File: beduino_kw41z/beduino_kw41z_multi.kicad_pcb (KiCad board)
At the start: 2 copper layers, 81 x 100 mm, 336 parts, among them J1 USB_OTG, J2 Conn_01x07, J3 Conn_01x07, Q1 Q_PMOS_SGD, SW1 SW_Push, SW2 Reset, U1 TC1017, U2 LPC11U35FHI33-501, U3 TC1017, U4 Module_CONN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

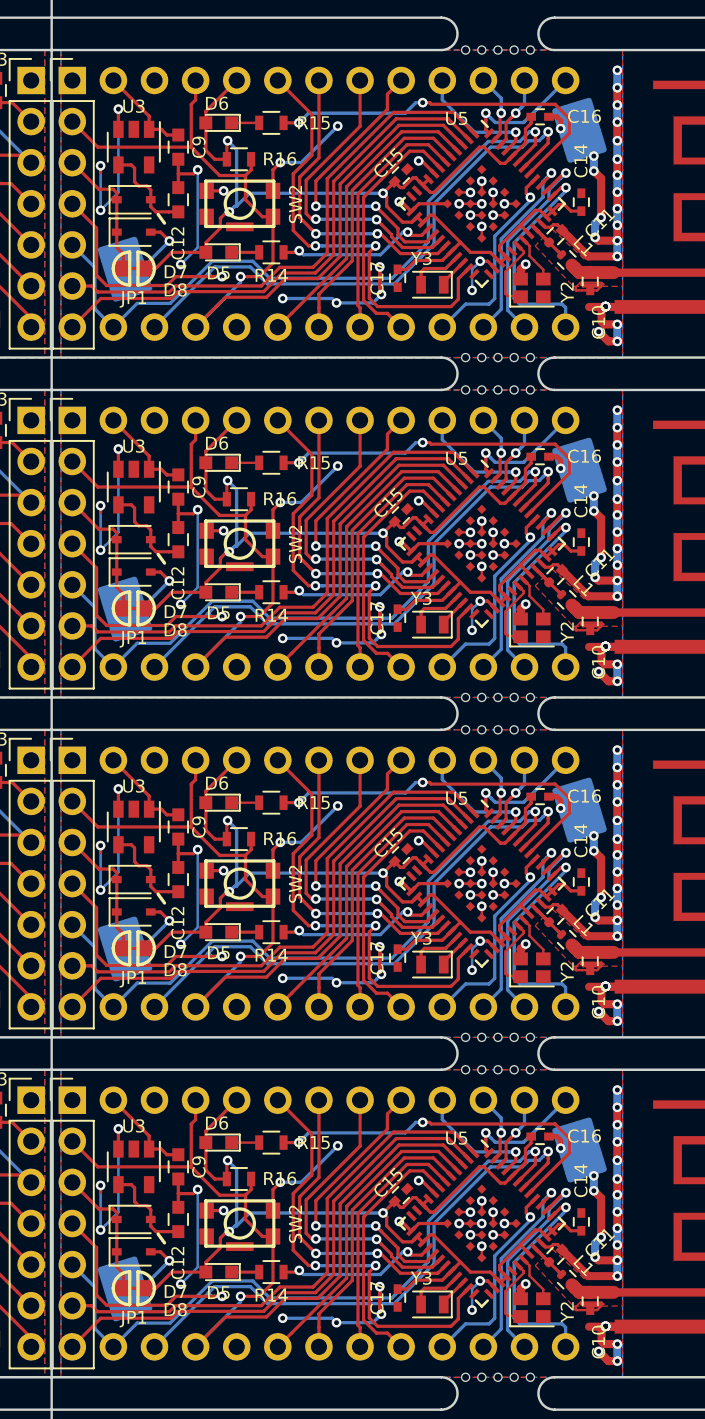
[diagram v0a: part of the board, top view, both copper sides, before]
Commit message: Update board design to be kicad v4 compatible again.
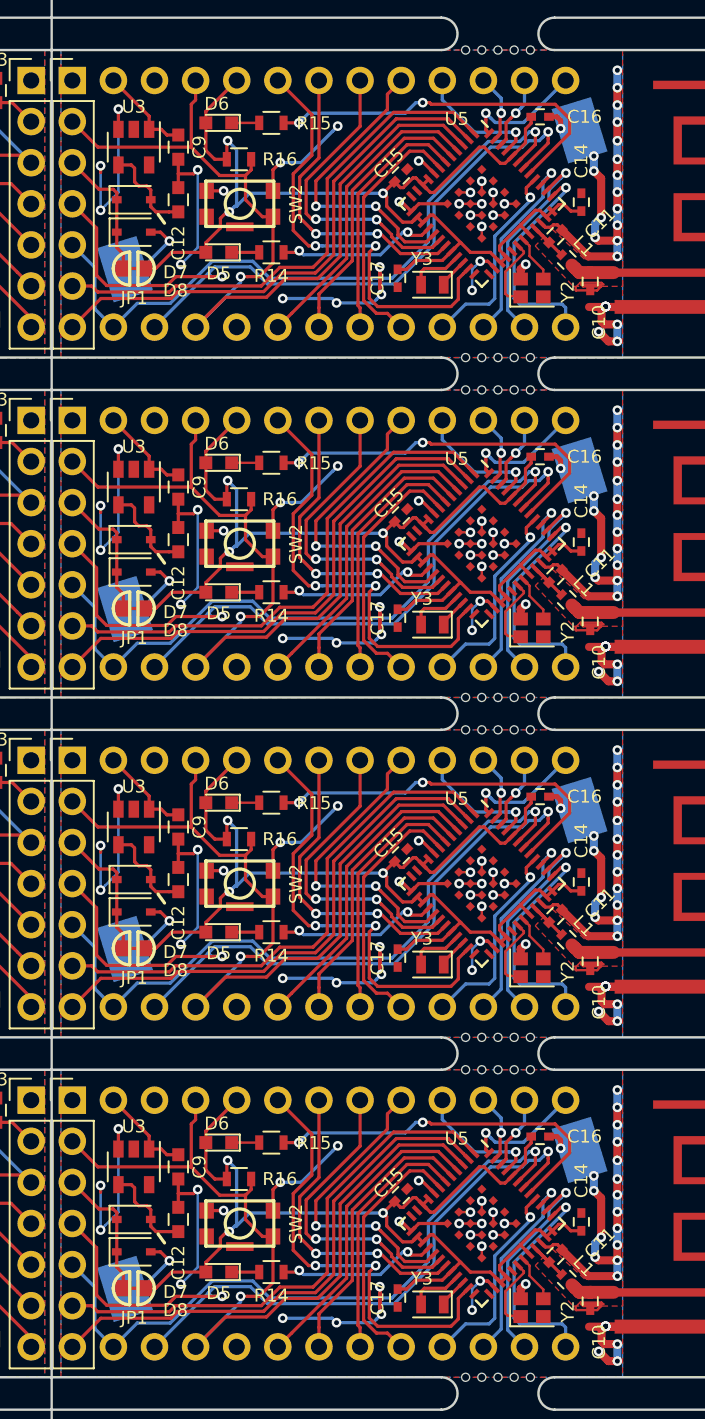
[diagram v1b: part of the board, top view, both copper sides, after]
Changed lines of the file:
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@@
     (fp_arc (start 0 0) (end -11.06 4.11) (angle -139.2) (layer B.CrtYd) (width 0.05))
     (fp_arc (start 0 0) (end 11.06 -4.11) (angle -139.2) (layer B.CrtYd) (width 0.05))
-    (pad 2 smd roundrect (at 14.68 0 17) (size 2.54 3.51) (layers B.Cu B.Paste B.Mask)(roundrect_rratio 0.07000000000000001)
+    (pad 2 smd rect (at 14.68 0 17) (size 2.54 3.51) (layers B.Cu B.Paste B.Mask)
       (zone_connect 2) (thermal_width 3.5) (thermal_gap 0.4))
-    (pad 1 smd roundrect (at -14.68 0 17) (size 2.54 3.51) (layers B.Cu B.Paste B.Mask)(roundrect_rratio 0.07000000000000001))
+    (pad 1 smd rect (at -14.68 0 17) (size 2.54 3.51) (layers B.Cu B.Paste B.Mask))
   )
   (module Housings_DFN_QFN:QFN-48-1EP_7x7mm_Pitch0.5mm (layer F.Cu)
@@
     (pad 1 smd rect (at -1.3 -1.35) (size 1.35 0.4) (layers F.Cu F.Paste F.Mask))
     (model ${KISYS3DMOD}/Connectors_USB.3dshapes/USB_Micro-B_Molex_47346-0001.step
-      (offset (xyz 0 -1.4 0))
+      (at (xyz 0 -1.4 0))
       (scale (xyz 1 1 1))
       (rotate (xyz 0 0 0))
@@
     (fp_line (start 1 0.4) (end 1 -0.4) (layer F.CrtYd) (width 0.05))
     (fp_line (start 1 0.4) (end -1 0.4) (layer F.CrtYd) (width 0.05))
-    (pad 1 smd roundrect (at -0.55 0 45) (size 0.6 0.5) (layers F.Cu F.Paste F.Mask)(roundrect_rratio 0.35))
+    (pad 1 smd rect (at -0.55 0 45) (size 0.6 0.5) (layers F.Cu F.Paste F.Mask))
     (pad 2 smd rect (at 0.55 0 45) (size 0.6 0.5) (layers F.Cu F.Paste F.Mask))
     (model Capacitors_SMD.3dshapes/C_0402.wrl
@@
     (fp_line (start 1 0.4) (end 1 -0.4) (layer F.CrtYd) (width 0.05))
     (fp_line (start 1 0.4) (end -1 0.4) (layer F.CrtYd) (width 0.05))
-    (pad 1 smd roundrect (at -0.55 0 270) (size 0.6 0.5) (layers F.Cu F.Paste F.Mask)(roundrect_rratio 0.35))
+    (pad 1 smd rect (at -0.55 0 270) (size 0.6 0.5) (layers F.Cu F.Paste F.Mask))
     (pad 2 smd rect (at 0.55 0 270) (size 0.6 0.5) (layers F.Cu F.Paste F.Mask))
     (model Capacitors_SMD.3dshapes/C_0402.wrl
@@
     (fp_line (start 0.25 -0.53) (end -0.25 -0.53) (layer F.SilkS) (width 0.12))
     (fp_line (start -0.25 0.53) (end 0.25 0.53) (layer F.SilkS) (width 0.12))
-    (pad 1 smd roundrect (at -0.45 0 315) (size 0.4 0.6) (layers F.Cu F.Paste F.Mask)(roundrect_rratio 0.35))
-    (pad 2 smd roundrect (at 0.45 0 315) (size 0.4 0.6) (layers F.Cu F.Paste F.Mask)(roundrect_rratio 0.35))
+    (pad 1 smd rect (at -0.45 0 315) (size 0.4 0.6) (layers F.Cu F.Paste F.Mask))
+    (pad 2 smd rect (at 0.45 0 315) (size 0.4 0.6) (layers F.Cu F.Paste F.Mask))
     (model ${KISYS3DMOD}/Inductors_SMD.3dshapes/L_0402.wrl
       (at (xyz 0 0 0))
@@
     (fp_arc (start 0 0) (end -11.06 4.11) (angle -139.2) (layer B.CrtYd) (width 0.05))
     (fp_arc (start 0 0) (end 11.06 -4.11) (angle -139.2) (layer B.CrtYd) (width 0.05))
-    (pad 2 smd roundrect (at 14.68 0 17) (size 2.54 3.51) (layers B.Cu B.Paste B.Mask)(roundrect_rratio 0.07000000000000001)
+    (pad 2 smd rect (at 14.68 0 17) (size 2.54 3.51) (layers B.Cu B.Paste B.Mask)
       (zone_connect 2) (thermal_width 3.5) (thermal_gap 0.4))
-    (pad 1 smd roundrect (at -14.68 0 17) (size 2.54 3.51) (layers B.Cu B.Paste B.Mask)(roundrect_rratio 0.07000000000000001))
+    (pad 1 smd rect (at -14.68 0 17) (size 2.54 3.51) (layers B.Cu B.Paste B.Mask))
   )
   (module Housings_DFN_QFN:QFN-48-1EP_7x7mm_Pitch0.5mm (layer F.Cu)
@@
     (pad 1 smd rect (at -1.3 -1.35) (size 1.35 0.4) (layers F.Cu F.Paste F.Mask))
     (model ${KISYS3DMOD}/Connectors_USB.3dshapes/USB_Micro-B_Molex_47346-0001.step
-      (offset (xyz 0 -1.4 0))
+      (at (xyz 0 -1.4 0))
       (scale (xyz 1 1 1))
       (rotate (xyz 0 0 0))
@@
     (fp_line (start 1 0.4) (end 1 -0.4) (layer F.CrtYd) (width 0.05))
     (fp_line (start 1 0.4) (end -1 0.4) (layer F.CrtYd) (width 0.05))
-    (pad 1 smd roundrect (at -0.55 0 45) (size 0.6 0.5) (layers F.Cu F.Paste F.Mask)(roundrect_rratio 0.35))
+    (pad 1 smd rect (at -0.55 0 45) (size 0.6 0.5) (layers F.Cu F.Paste F.Mask))
     (pad 2 smd rect (at 0.55 0 45) (size 0.6 0.5) (layers F.Cu F.Paste F.Mask))
     (model Capacitors_SMD.3dshapes/C_0402.wrl
@@
     (fp_line (start 1 0.4) (end 1 -0.4) (layer F.CrtYd) (width 0.05))
     (fp_line (start 1 0.4) (end -1 0.4) (layer F.CrtYd) (width 0.05))
-    (pad 1 smd roundrect (at -0.55 0 270) (size 0.6 0.5) (layers F.Cu F.Paste F.Mask)(roundrect_rratio 0.35))
+    (pad 1 smd rect (at -0.55 0 270) (size 0.6 0.5) (layers F.Cu F.Paste F.Mask))
     (pad 2 smd rect (at 0.55 0 270) (size 0.6 0.5) (layers F.Cu F.Paste F.Mask))
     (model Capacitors_SMD.3dshapes/C_0402.wrl
@@
     (fp_line (start 0.25 -0.53) (end -0.25 -0.53) (layer F.SilkS) (width 0.12))
     (fp_line (start -0.25 0.53) (end 0.25 0.53) (layer F.SilkS) (width 0.12))
-    (pad 1 smd roundrect (at -0.45 0 315) (size 0.4 0.6) (layers F.Cu F.Paste F.Mask)(roundrect_rratio 0.35))
-    (pad 2 smd roundrect (at 0.45 0 315) (size 0.4 0.6) (layers F.Cu F.Paste F.Mask)(roundrect_rratio 0.35))
+    (pad 1 smd rect (at -0.45 0 315) (size 0.4 0.6) (layers F.Cu F.Paste F.Mask))
+    (pad 2 smd rect (at 0.45 0 315) (size 0.4 0.6) (layers F.Cu F.Paste F.Mask))
     (model ${KISYS3DMOD}/Inductors_SMD.3dshapes/L_0402.wrl
       (at (xyz 0 0 0))
@@
     (fp_arc (start 0 0) (end -11.06 4.11) (angle -139.2) (layer B.CrtYd) (width 0.05))
     (fp_arc (start 0 0) (end 11.06 -4.11) (angle -139.2) (layer B.CrtYd) (width 0.05))
-    (pad 2 smd roundrect (at 14.68 0 17) (size 2.54 3.51) (layers B.Cu B.Paste B.Mask)(roundrect_rratio 0.07000000000000001)
+    (pad 2 smd rect (at 14.68 0 17) (size 2.54 3.51) (layers B.Cu B.Paste B.Mask)
       (zone_connect 2) (thermal_width 3.5) (thermal_gap 0.4))
-    (pad 1 smd roundrect (at -14.68 0 17) (size 2.54 3.51) (layers B.Cu B.Paste B.Mask)(roundrect_rratio 0.07000000000000001))
+    (pad 1 smd rect (at -14.68 0 17) (size 2.54 3.51) (layers B.Cu B.Paste B.Mask))
   )
   (module Housings_DFN_QFN:QFN-48-1EP_7x7mm_Pitch0.5mm (layer F.Cu)
@@
     (pad 1 smd rect (at -1.3 -1.35) (size 1.35 0.4) (layers F.Cu F.Paste F.Mask))
     (model ${KISYS3DMOD}/Connectors_USB.3dshapes/USB_Micro-B_Molex_47346-0001.step
-      (offset (xyz 0 -1.4 0))
+      (at (xyz 0 -1.4 0))
       (scale (xyz 1 1 1))
       (rotate (xyz 0 0 0))
@@
     (fp_line (start 1 0.4) (end 1 -0.4) (layer F.CrtYd) (width 0.05))
     (fp_line (start 1 0.4) (end -1 0.4) (layer F.CrtYd) (width 0.05))
-    (pad 1 smd roundrect (at -0.55 0 45) (size 0.6 0.5) (layers F.Cu F.Paste F.Mask)(roundrect_rratio 0.35))
+    (pad 1 smd rect (at -0.55 0 45) (size 0.6 0.5) (layers F.Cu F.Paste F.Mask))
     (pad 2 smd rect (at 0.55 0 45) (size 0.6 0.5) (layers F.Cu F.Paste F.Mask))
     (model Capacitors_SMD.3dshapes/C_0402.wrl
@@
     (fp_line (start 1 0.4) (end 1 -0.4) (layer F.CrtYd) (width 0.05))
     (fp_line (start 1 0.4) (end -1 0.4) (layer F.CrtYd) (width 0.05))
-    (pad 1 smd roundrect (at -0.55 0 270) (size 0.6 0.5) (layers F.Cu F.Paste F.Mask)(roundrect_rratio 0.35))
+    (pad 1 smd rect (at -0.55 0 270) (size 0.6 0.5) (layers F.Cu F.Paste F.Mask))
     (pad 2 smd rect (at 0.55 0 270) (size 0.6 0.5) (layers F.Cu F.Paste F.Mask))
     (model Capacitors_SMD.3dshapes/C_0402.wrl
@@
     (fp_line (start 0.25 -0.53) (end -0.25 -0.53) (layer F.SilkS) (width 0.12))
     (fp_line (start -0.25 0.53) (end 0.25 0.53) (layer F.SilkS) (width 0.12))
-    (pad 1 smd roundrect (at -0.45 0 315) (size 0.4 0.6) (layers F.Cu F.Paste F.Mask)(roundrect_rratio 0.35))
-    (pad 2 smd roundrect (at 0.45 0 315) (size 0.4 0.6) (layers F.Cu F.Paste F.Mask)(roundrect_rratio 0.35))
+    (pad 1 smd rect (at -0.45 0 315) (size 0.4 0.6) (layers F.Cu F.Paste F.Mask))
+    (pad 2 smd rect (at 0.45 0 315) (size 0.4 0.6) (layers F.Cu F.Paste F.Mask))
     (model ${KISYS3DMOD}/Inductors_SMD.3dshapes/L_0402.wrl
       (at (xyz 0 0 0))
@@
     (fp_arc (start 0 0) (end -10.61275 3.5) (angle -27.4635) (layer B.Fab) (width 0.1))
     (fp_circle (center 0 0) (end 10 0) (layer Dwgs.User) (width 0.15))
-    (pad 1 smd roundrect (at -14.68 0 17) (size 2.54 3.51) (layers B.Cu B.Paste B.Mask)(roundrect_rratio 0.07000000000000001)
+    (pad 1 smd rect (at -14.68 0 17) (size 2.54 3.51) (layers B.Cu B.Paste B.Mask)
       (net 3 "Net-(BT1-Pad1)"))
-    (pad 2 smd roundrect (at 14.68 0 17) (size 2.54 3.51) (layers B.Cu B.Paste B.Mask)(roundrect_rratio 0.07000000000000001)
+    (pad 2 smd rect (at 14.68 0 17) (size 2.54 3.51) (layers B.Cu B.Paste B.Mask)
       (net 1 GND) (zone_connect 2) (thermal_width 3.5) (thermal_gap 0.4))
   )
@@
       (effects (font (size 0.2 0.2) (thickness 0.03)))
     )
-    (pad 2 smd roundrect (at 0.45 0 315) (size 0.4 0.6) (layers F.Cu F.Paste F.Mask)(roundrect_rratio 0.35)
+    (pad 2 smd rect (at 0.45 0 315) (size 0.4 0.6) (layers F.Cu F.Paste F.Mask)
       (net 2 "Net-(ANT1-Pad1)"))
-    (pad 1 smd roundrect (at -0.45 0 315) (size 0.4 0.6) (layers F.Cu F.Paste F.Mask)(roundrect_rratio 0.35)
+    (pad 1 smd rect (at -0.45 0 315) (size 0.4 0.6) (layers F.Cu F.Paste F.Mask)
       (net 10 /KW41Z/ANT))
     (model ${KISYS3DMOD}/Inductors_SMD.3dshapes/L_0402.wrl
@@
     (pad 2 smd rect (at 0.55 0 270) (size 0.6 0.5) (layers F.Cu F.Paste F.Mask)
       (net 1 GND))
-    (pad 1 smd roundrect (at -0.55 0 270) (size 0.6 0.5) (layers F.Cu F.Paste F.Mask)(roundrect_rratio 0.35)
+    (pad 1 smd rect (at -0.55 0 270) (size 0.6 0.5) (layers F.Cu F.Paste F.Mask)
       (net 2 "Net-(ANT1-Pad1)"))
     (model Capacitors_SMD.3dshapes/C_0402.wrl
@@
     (pad 2 smd rect (at 0.55 0 45) (size 0.6 0.5) (layers F.Cu F.Paste F.Mask)
       (net 1 GND))
-    (pad 1 smd roundrect (at -0.55 0 45) (size 0.6 0.5) (layers F.Cu F.Paste F.Mask)(roundrect_rratio 0.35)
+    (pad 1 smd rect (at -0.55 0 45) (size 0.6 0.5) (layers F.Cu F.Paste F.Mask)
       (net 10 /KW41Z/ANT))
     (model Capacitors_SMD.3dshapes/C_0402.wrl
@@
       (net 1 GND))
     (model ${KISYS3DMOD}/Connectors_USB.3dshapes/USB_Micro-B_Molex_47346-0001.step
-      (offset (xyz 0 -1.4 0))
+      (at (xyz 0 -1.4 0))
       (scale (xyz 1 1 1))
       (rotate (xyz 0 0 0))
